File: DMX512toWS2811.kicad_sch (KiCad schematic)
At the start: 74 parts, among them IC1 MAX485ESA+, IC2 MAX485ESA+, IC3 YDS-205, IC4 TLP2361_TPL,E, IC5 MAX485ESA+, IC6 PIC18F27Q43-I_SO, IC7 HD74LV541AT-E, J1 7810-8P8C, J2 7810-8P8C, J3 7810-8P8C, J4 18742, J5 TB112-2-2-E-1, J6 TB112-2-2-E-1, J7 TB111-2-3-U-1-1, U1 FUC-03A, U2 FUC-03A, U3 ERZV07D220, X1 CXO_DIP8

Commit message: * バッテリー監視追加
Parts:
- added C19: 100u, symbol Device:C_Polarized
- added J8: B6B-PH-K-S_LF__SN_, SHDR6W50P0X200_1X6_1390X450X600P, symbol SamacSys_Parts:B6B-PH-K-S_LF__SN_
- added J9: TB112-2-2-E-1, TB11222E1, symbol SamacSys_Parts:TB112-2-2-E-1
- added PS2: BP5293-50, TO254P570X1700X1780-3P, symbol SamacSys_Parts:BP5293-50
- added R22, R23: 1k, symbol Device:R
- added TP1, TP12, TP13, TP14, TP15, TP16, TP17, TP2, TP3, TP4, TP5, TP6, TP7, TP9: TestPoint, symbol Connector:TestPoint
- R1, R16, R2, R20, R5, R6, R7: value R -> 100
- R10, R12, R14, R18: value R -> 1k
- R15, R17, R19, R21, R3, R4, R9: value R -> 10k
- R8: value R -> 300
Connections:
- net +5V: now also J8.2, PS2.3 (VOUT)
- net +BATT: now also J9.1
- net GND: now also C18.1, C2.1, C3.1, IC3.1 (VIN), J5.1, L3.2, LED2.1, C19.2, J8.3, J9.2, PS2.1 (VIN), PS2.2 (GND), R22.1, R23.2
- net ICSPCLK: now also J8.5
- net ICSPDAT: now also J8.4
- net RESET: now also J8.1
- net at IC7.1 (~{OE1}), R19.2: now also IC6.15 (RC4)
- net at C6.1, C7.1, L1.1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: now also C19.1
- net at IC6.10 (RA6): now also TP7.1
- net at IC6.11 (RC0): now also R22.2, R23.1
- net at IC6.12 (RC1): now also TP9.1
- net at IC6.13 (RC2): now also R12.1
- net at IC6.14 (RC3): now also R14.2
- net at IC6.2 (RA0): now also TP1.1
- net at IC6.21 (RB0): now also TP12.1
- net at IC6.22 (RB1): now also TP13.1
- net at IC6.23 (RB2): now also TP14.1
- net at IC6.24 (RB3): now also TP15.1
- net at IC6.25 (RB4): now also TP16.1
- net at IC6.26 (RB5): now also TP17.1
- net at IC6.3 (RA1): now also TP2.1
- net at IC6.4 (RA2): now also TP3.1
- net at IC6.5 (RA3): now also TP4.1
- net at IC6.6 (RA4): now also TP5.1
- net at IC6.7 (RA5): now also TP6.1
- net VDC: no longer names the net of L3.1, U2.1, U2.2, U3.1
- net VDC: no longer C18.1, J5.1
- no-connect marks 25 -> 26
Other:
- moved on the sheet: L1, LED2, LED4, R12, R14, R19, S1, S2

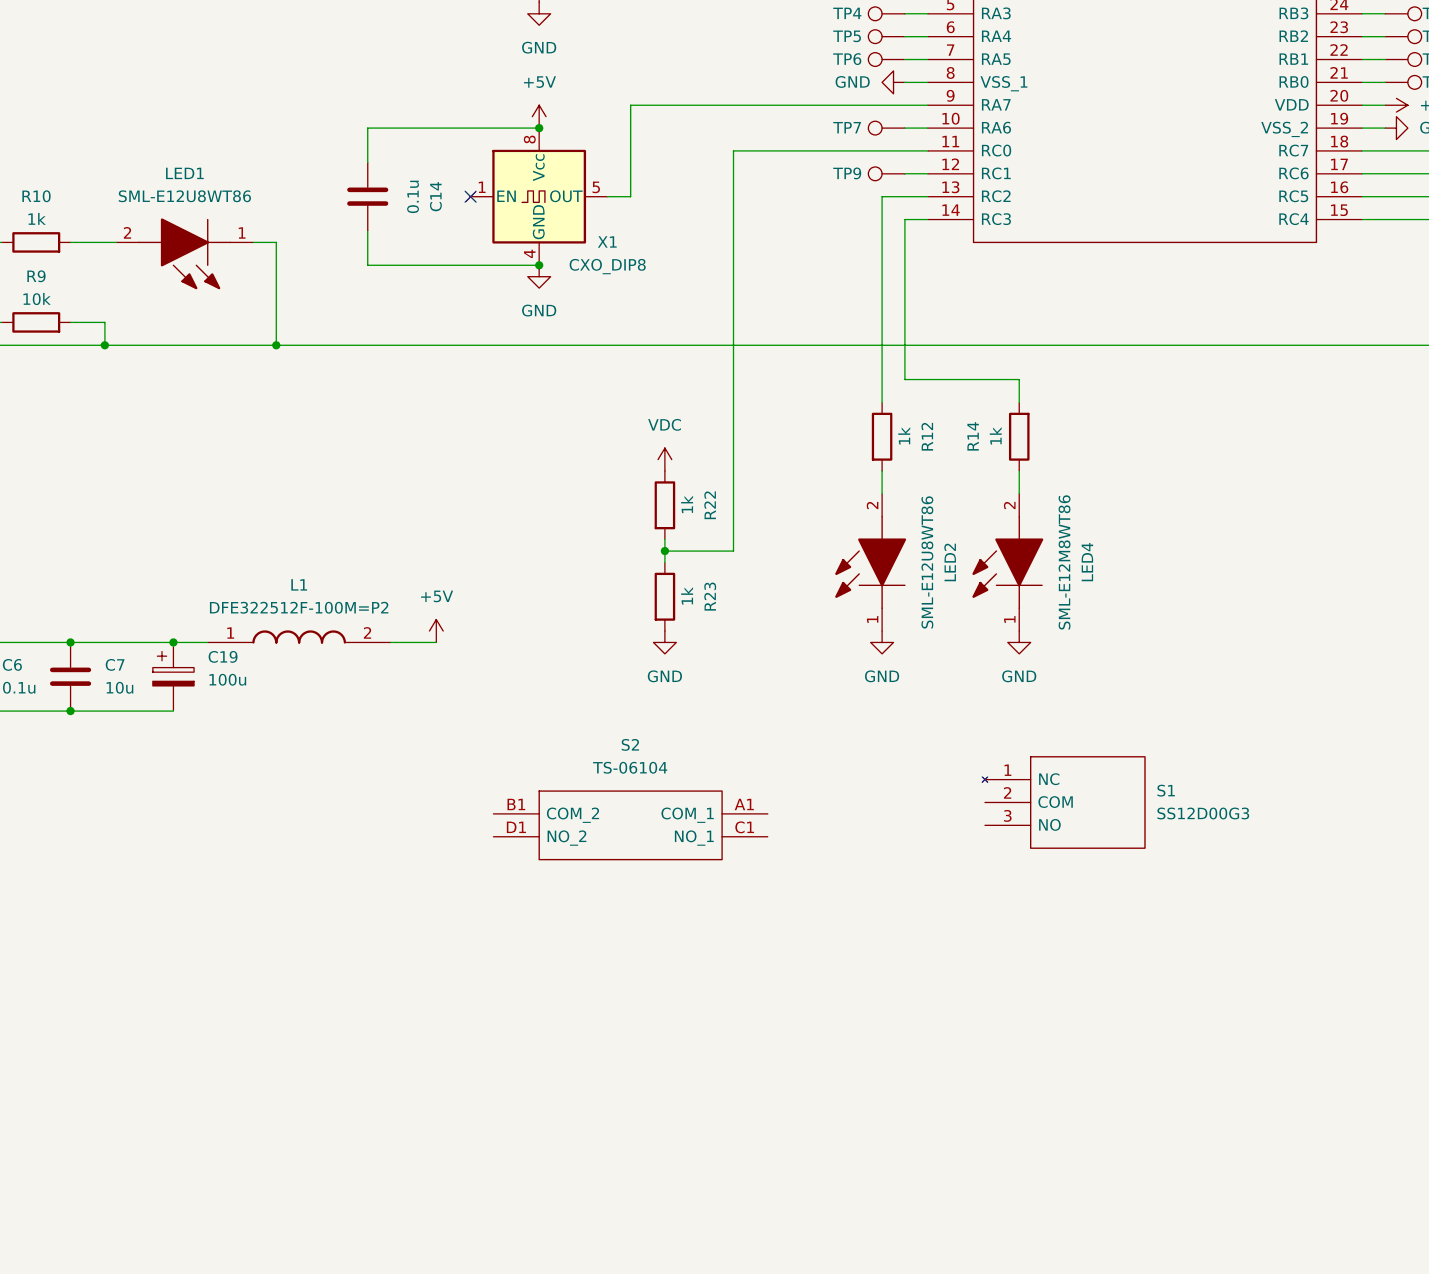
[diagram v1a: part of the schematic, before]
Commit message: * 動作モード切り替えスイッチの追加
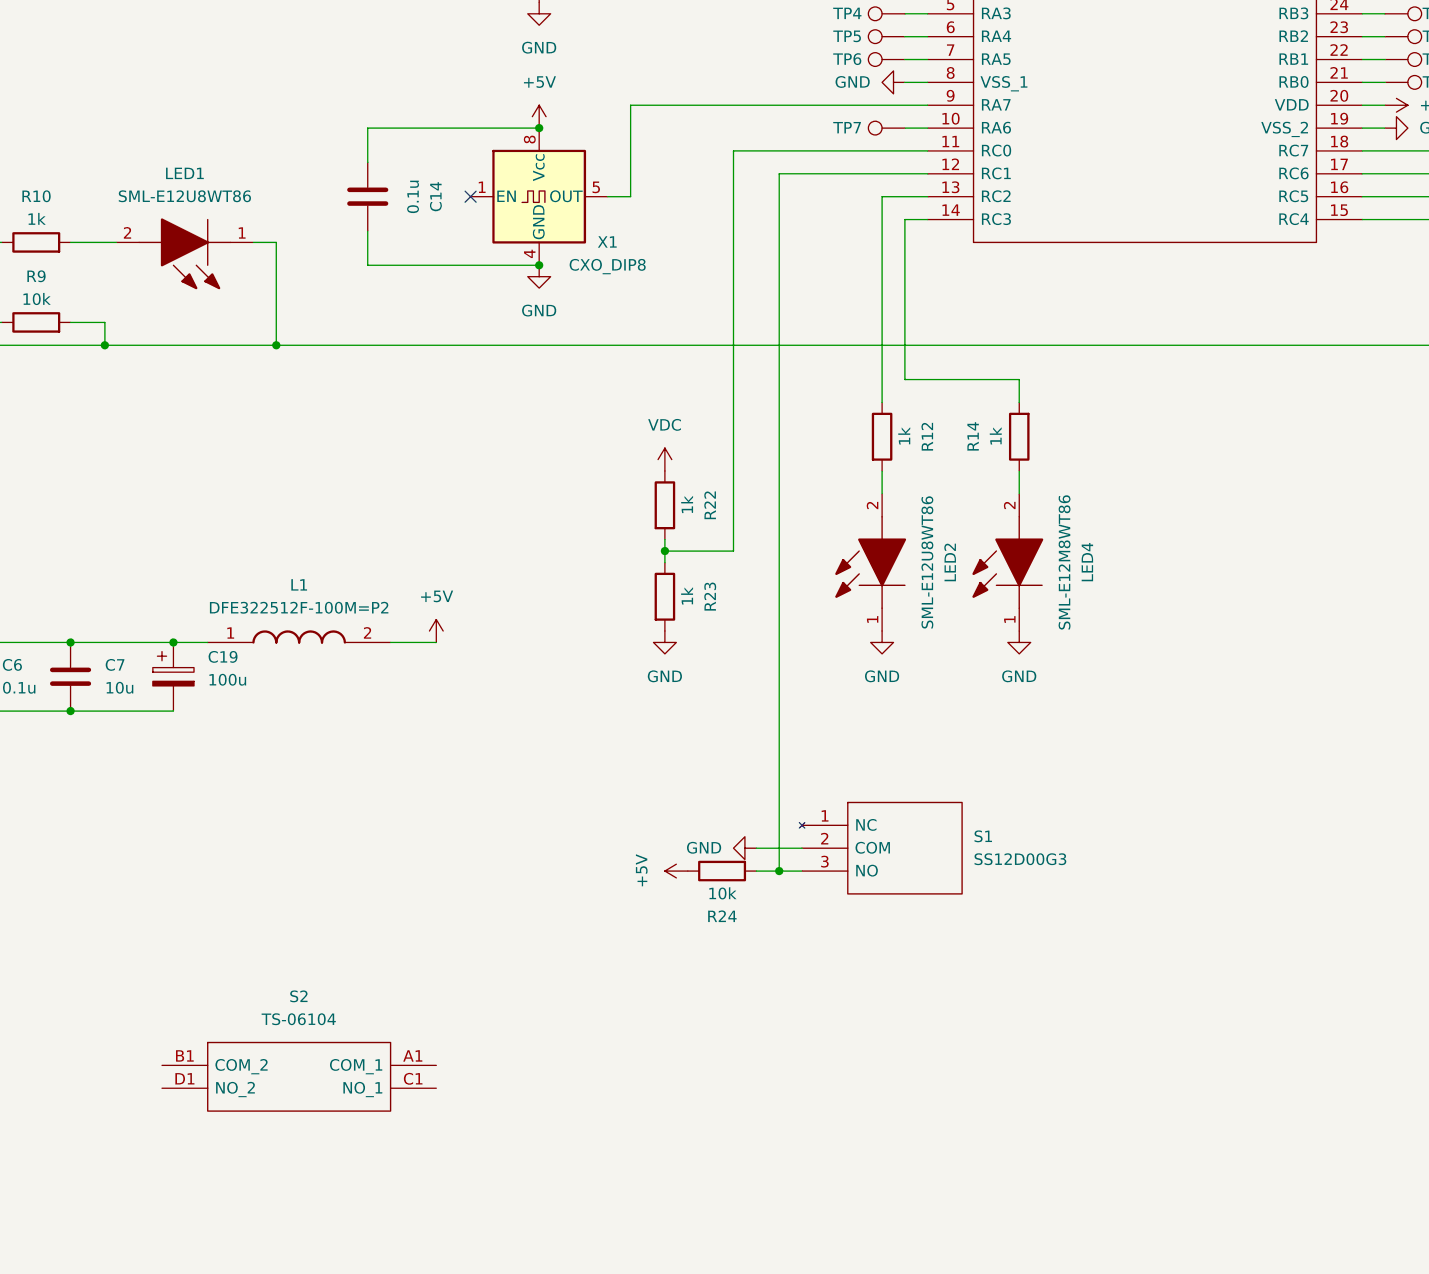
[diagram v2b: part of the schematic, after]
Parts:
- removed TP9: TestPoint, symbol Connector:TestPoint
- added R24: 10k, symbol Device:R
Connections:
- net +5V: now also R24.1
- net GND: now also S1.2 (COM)
- net at IC6.12 (RC1): now also S1.3 (NO), R24.2
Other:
- moved on the sheet: S1, S2

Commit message: * 外部電源供給回路にSWを追加     * MOSFETに逆流時の寄生ダイオード保護のためのダイオードを追加したほうがいいかも * リセットSW､モード切り替えSWを修正
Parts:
- removed C17: 1000u, symbol Device:C_Polarized
- removed TP1, TP12, TP13: TestPoint, symbol Connector:TestPoint
- added C20: 1000u, symbol Device:C_Polarized
- added Q1, Q2: TJ60S04M3L, TJ60S04M3L, symbol SamacSys_Parts:TJ60S04M3L
- added R25: 10k, symbol Device:R
- added R26, R29: 100, symbol Device:R
- added R27, R28, R30: 100k, symbol Device:R
- R13: value R -> 1k
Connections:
- net +5V: now also R25.1; no longer J7.1
- net GND: now also S2.C1 (NO_1), S2.D1 (NO_2), C20.1, C20.2, Q1.3 (S), Q2.3 (S), R27.1, R28.1, R30.2; no longer J5.1
- net at R22.2, R23.1: now also IC6.2 (RA0); no longer IC6.11 (RC0)
- net at IC6.21 (RB0): now also R26.1
- net at IC6.22 (RB1): now also R29.1
- net at S2.A1 (COM_1): now also IC6.11 (RC0), S2.B1 (COM_2), R25.2
- new net: Q2.1 (G), R28.2, R29.2, R30.1
- new net: J5.1, Q2.2 (D)
- new net: Q1.1 (G), R26.2, R27.2
- new net: J7.1, Q1.2 (D)
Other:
- moved on the sheet: C1, C10, C11, C12, C13, C14, C15, C16, C18, C19, C2, C3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

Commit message: * 大まかに配線完了
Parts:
- removed C2, C20: 1000u, symbol Device:C_Polarized
- removed IC3: YDS-205, YDS205, symbol SamacSys_Parts:YDS-205
- removed L3: DFE322512F-100M=P2, 1277ASH100MP2, symbol SamacSys_Parts:DFE322512F-100M=P2
- removed PS2: BP5293-50, TO254P570X1700X1780-3P, symbol SamacSys_Parts:BP5293-50
- removed R20: 100, symbol Device:R
- removed TP15, TP16, TP17, TP3, TP7: TestPoint, symbol Connector:TestPoint
- added C13, C14, C15, C16: 0.1u, Capacitor_SMD:C_0603_1608Metric_Pad1.08x0.95mm_HandSolder, symbol Device:C
- added C6: 4700p, Capacitor_THT:C_Disc_D12.5mm_W5.0mm_P10.00mm, symbol Device:C
- added CA1: 330u, Capacitor_THT:CP_Radial_D10.0mm_P5.00mm, symbol Device:C_Polarized
- added CA4: 1000u, Capacitor_THT:CP_Radial_D10.0mm_P5.00mm, symbol Device:C_Polarized
- added D4: SMBJ5.0CA, DIONM5436X261N, symbol SamacSys_Parts:SMBJ5.0CA
- added D6, D8: SBR2U30P1-7, SODFL3718X100N, symbol SamacSys_Parts:SBR2U30P1-7
- added F3: NANOSMDC010F-2, FUSC3216X100N, symbol SamacSys_Parts:NANOSMDC010F-2
- added F4, F7: FUC-03A, FUC03A, symbol SamacSys_Parts:FUC-03A
- added FL1, FL2: DLW21SN261SQ2L, DLW21SN121HQ2L, symbol SamacSys_Parts:DLW21SN261SQ2L
- added FL3: BNX022-01B, BNX02201K, symbol SamacSys_Parts:BNX022-01B
- added IC4: TCK106AF,LF, SMV_1, symbol SamacSys_Parts:TCK106AF,LF
- added LED1: SML-E12M8WT86, LEDC1608X46N, symbol SamacSys_Parts:SML-E12M8WT86
- added LED6: OSTBABS4C2B, OSTBABS4C2B, symbol SamacSys_Parts:OSTBABS4C2B
- added NT1, NT2: NetTie_2, NetTie:NetTie-2_SMD_Pad2.0mm, symbol Device:NetTie_2
- added PS2: NID35-5, NID355, symbol SamacSys_Parts:NID35-5
- added Q2: 2SK1062_F_, SSM3K7002CFULF, symbol SamacSys_Parts:2SK1062_F_
- added R11: 150k, Resistor_SMD:R_0603_1608Metric_Pad0.98x0.95mm_HandSolder, symbol Device:R
- added R13, R22, R23, R26, R27, R28: 1k, Resistor_SMD:R_0603_1608Metric_Pad0.98x0.95mm_HandSolder, symbol Device:R
- added R17, R33: 10k, Resistor_SMD:R_0603_1608Metric_Pad0.98x0.95mm_HandSolder, symbol Device:R
- added R34: 100, Resistor_SMD:R_1206_3216Metric_Pad1.30x1.75mm_HandSolder, symbol Device:R
- added R40: 100k, Resistor_SMD:R_0603_1608Metric_Pad0.98x0.95mm_HandSolder, symbol Device:R
- C1: renamed from C12; footprint (none) -> Capacitor_SMD:C_0603_1608Metric_Pad1.08x0.95mm_HandSolder; Manufacturer_Name (none) -> murata; Manufacturer_Part_Number (none) -> GRM188F11H104ZA01
- C10: renamed from C4; footprint (none) -> Capacitor_SMD:C_0603_1608Metric_Pad1.08x0.95mm_HandSolder; Manufacturer_Name (none) -> murata; Manufacturer_Part_Number (none) -> GRM188F11H104ZA01
- C11: renamed from C14; footprint (none) -> Capacitor_SMD:C_0603_1608Metric_Pad1.08x0.95mm_HandSolder; Manufacturer_Name (none) -> murata; Manufacturer_Part_Number (none) -> GRM188F11H104ZA01
- C12: renamed from C13; footprint (none) -> Capacitor_SMD:C_0603_1608Metric_Pad1.08x0.95mm_HandSolder; Manufacturer_Name (none) -> murata; Manufacturer_Part_Number (none) -> GRM188F11H104ZA01
- C17: renamed from C5; footprint (none) -> Capacitor_SMD:C_0603_1608Metric_Pad1.08x0.95mm_HandSolder; Manufacturer_Name (none) -> murata; Manufacturer_Part_Number (none) -> GRM188F11H104ZA01
- C18: renamed from C16; footprint (none) -> Capacitor_SMD:C_0603_1608Metric_Pad1.08x0.95mm_HandSolder; Manufacturer_Name (none) -> murata; Manufacturer_Part_Number (none) -> GRM188F11H104ZA01
- C19: renamed from C15; footprint (none) -> Capacitor_SMD:C_0603_1608Metric_Pad1.08x0.95mm_HandSolder; Manufacturer_Name (none) -> murata; Manufacturer_Part_Number (none) -> GRM188F11H104ZA01
- C2: renamed from C11; footprint (none) -> Capacitor_SMD:C_0603_1608Metric_Pad1.08x0.95mm_HandSolder; Manufacturer_Name (none) -> murata; Manufacturer_Part_Number (none) -> GRM188F11H104ZA01
- C3: renamed from C8; footprint (none) -> Capacitor_SMD:C_0603_1608Metric_Pad1.08x0.95mm_HandSolder; Manufacturer_Name (none) -> murata; Manufacturer_Part_Number (none) -> GRM188F11H104ZA01
- C4: renamed from C9; footprint (none) -> Capacitor_SMD:C_1206_3216Metric_Pad1.33x1.80mm_HandSolder; Manufacturer_Name (none) -> murata; Manufacturer_Part_Number (none) -> GRM31CB31H106KA12
- C5: renamed from C10; footprint (none) -> Capacitor_SMD:C_0603_1608Metric_Pad1.08x0.95mm_HandSolder; Manufacturer_Name (none) -> murata; Manufacturer_Part_Number (none) -> GRM188F11H104ZA01
- C7: renamed from C6; footprint (none) -> Capacitor_SMD:C_0603_1608Metric_Pad1.08x0.95mm_HandSolder; Manufacturer_Name (none) -> murata; Manufacturer_Part_Number (none) -> GRM188F11H104ZA01
- C8: renamed from C3; footprint (none) -> Capacitor_SMD:C_0603_1608Metric_Pad1.08x0.95mm_HandSolder; Manufacturer_Name (none) -> murata; Manufacturer_Part_Number (none) -> GRM188F11H104ZA01
- C9: renamed from C7; footprint (none) -> Capacitor_SMD:C_1206_3216Metric_Pad1.33x1.80mm_HandSolder; Manufacturer_Name (none) -> murata; Manufacturer_Part_Number (none) -> GRM31CB31H106KA12
- CA2: renamed from C19; footprint (none) -> Capacitor_THT:CP_Radial_D6.3mm_P2.50mm; Manufacturer_Name (none) -> Panasonic; Manufacturer_Part_Number (none) -> 16SEPC100M
- CA3: renamed from C1; value 1000u -> 22u; footprint (none) -> Capacitor_THT:CP_Radial_D6.3mm_P2.50mm; Manufacturer_Name (none) -> Panasonic; Manufacturer_Part_Number (none) -> 35SEPF22M
- CA5: renamed from C18; value 1000u -> 330u; footprint (none) -> Capacitor_THT:CP_Radial_D10.0mm_P5.00mm; Manufacturer_Name (none) -> Rubycon; Manufacturer_Part_Number (none) -> 35PZJ330M10X9
- D3: Manufacturer_Name (none) -> ROHM; Manufacturer_Part_Number (none) -> 1SS355VM
- IC3: renamed from IC4; footprint 11-4L1S(5-PIN-SOIC) -> SamacSys_Parts:11-4L1S_5-PIN-SOIC_
- LED2: renamed from LED1; footprint LEDM168X46N -> LEDC1608X46N
- LED4: renamed from LED2; footprint LEDM168X46N -> LEDC1608X46N
- R1, R2: footprint (none) -> Resistor_SMD:R_1206_3216Metric_Pad1.30x1.75mm_HandSolder; Manufacturer_Name (none) -> susumu; Manufacturer_Part_Number (none) -> RG3216P-1000-B-T5
- R10: renamed from R11; footprint (none) -> Resistor_SMD:R_0805_2012Metric_Pad1.20x1.40mm_HandSolder; Manufacturer_Name (none) -> FAITHFUL LINK INDUSTRIAL CORP.; Manufacturer_Part_Number (none) -> RC0603J240R
- R12: renamed from R8; footprint (none) -> Resistor_SMD:R_0603_1608Metric_Pad0.98x0.95mm_HandSolder; Manufacturer_Name (none) -> FAITHFUL LINK INDUSTRIAL CORP.; Manufacturer_Part_Number (none) -> RC0603J300R
- R14: renamed from R10; footprint (none) -> Resistor_SMD:R_0603_1608Metric_Pad0.98x0.95mm_HandSolder; Manufacturer_Name (none) -> FAITHFUL LINK INDUSTRIAL CORP.; Manufacturer_Part_Number (none) -> RC0603J1K
- R15: renamed from R9; footprint (none) -> Resistor_SMD:R_0603_1608Metric_Pad0.98x0.95mm_HandSolder; Manufacturer_Name (none) -> FAITHFUL LINK INDUSTRIAL CORP.; Manufacturer_Part_Number (none) -> RC0603J10K
- R16: renamed from R25; footprint (none) -> Resistor_SMD:R_0603_1608Metric_Pad0.98x0.95mm_HandSolder; Manufacturer_Name (none) -> FAITHFUL LINK INDUSTRIAL CORP.; Manufacturer_Part_Number (none) -> RC0603J10K
- R18: renamed from R15; footprint (none) -> Resistor_SMD:R_0603_1608Metric_Pad0.98x0.95mm_HandSolder; Manufacturer_Name (none) -> FAITHFUL LINK INDUSTRIAL CORP.; Manufacturer_Part_Number (none) -> RC0603J10K
- R19: renamed from R13; footprint (none) -> Resistor_SMD:R_0603_1608Metric_Pad0.98x0.95mm_HandSolder; Manufacturer_Name (none) -> FAITHFUL LINK INDUSTRIAL CORP.; Manufacturer_Part_Number (none) -> RC0603J1K
- R20: renamed from R16; footprint (none) -> Resistor_SMD:R_0603_1608Metric_Pad0.98x0.95mm_HandSolder; Manufacturer_Name (none) -> FAITHFUL LINK INDUSTRIAL CORP.; Manufacturer_Part_Number (none) -> RC0603J100R
- R21: renamed from R24; footprint (none) -> Resistor_SMD:R_0603_1608Metric_Pad0.98x0.95mm_HandSolder; Manufacturer_Name (none) -> FAITHFUL LINK INDUSTRIAL CORP.; Manufacturer_Part_Number (none) -> RC0603J10K
- R24: renamed from R12; footprint (none) -> Resistor_SMD:R_0603_1608Metric_Pad0.98x0.95mm_HandSolder; Manufacturer_Name (none) -> FAITHFUL LINK INDUSTRIAL CORP.; Manufacturer_Part_Number (none) -> RC0603J1K
- R25: renamed from R14; footprint (none) -> Resistor_SMD:R_0603_1608Metric_Pad0.98x0.95mm_HandSolder; Manufacturer_Name (none) -> FAITHFUL LINK INDUSTRIAL CORP.; Manufacturer_Part_Number (none) -> RC0603J1K
- R29: renamed from R21; footprint (none) -> Resistor_SMD:R_0603_1608Metric_Pad0.98x0.95mm_HandSolder; Manufacturer_Name (none) -> FAITHFUL LINK INDUSTRIAL CORP.; Manufacturer_Part_Number (none) -> RC0603J10K
- R3: renamed from R5; footprint (none) -> Resistor_SMD:R_1206_3216Metric_Pad1.30x1.75mm_HandSolder; Manufacturer_Name (none) -> susumu; Manufacturer_Part_Number (none) -> RG3216P-1000-B-T5
- R30: renamed from R19; footprint (none) -> Resistor_SMD:R_0603_1608Metric_Pad0.98x0.95mm_HandSolder; Manufacturer_Name (none) -> FAITHFUL LINK INDUSTRIAL CORP.; Manufacturer_Part_Number (none) -> RC0603J10K
- R31: renamed from R18; footprint (none) -> Resistor_SMD:R_0603_1608Metric_Pad0.98x0.95mm_HandSolder; Manufacturer_Name (none) -> FAITHFUL LINK INDUSTRIAL CORP.; Manufacturer_Part_Number (none) -> RC0603J1K
- R32: renamed from R17; footprint (none) -> Resistor_SMD:R_0603_1608Metric_Pad0.98x0.95mm_HandSolder; Manufacturer_Name (none) -> FAITHFUL LINK INDUSTRIAL CORP.; Manufacturer_Part_Number (none) -> RC0603J10K
- R35: renamed from R26; footprint (none) -> Resistor_SMD:R_0603_1608Metric_Pad0.98x0.95mm_HandSolder; Manufacturer_Name (none) -> FAITHFUL LINK INDUSTRIAL CORP.; Manufacturer_Part_Number (none) -> RC0603J100R
- R36: renamed from R27; footprint (none) -> Resistor_SMD:R_0603_1608Metric_Pad0.98x0.95mm_HandSolder; Manufacturer_Name (none) -> FAITHFUL LINK INDUSTRIAL CORP.; Manufacturer_Part_Number (none) -> RC0603J100K
- R37: renamed from R29; footprint (none) -> Resistor_SMD:R_0603_1608Metric_Pad0.98x0.95mm_HandSolder; Manufacturer_Name (none) -> FAITHFUL LINK INDUSTRIAL CORP.; Manufacturer_Part_Number (none) -> RC0603J100R
- R38: renamed from R30; footprint (none) -> Resistor_SMD:R_0603_1608Metric_Pad0.98x0.95mm_HandSolder; Manufacturer_Name (none) -> FAITHFUL LINK INDUSTRIAL CORP.; Manufacturer_Part_Number (none) -> RC0603J100K
- R39: renamed from R28; footprint (none) -> Resistor_SMD:R_0603_1608Metric_Pad0.98x0.95mm_HandSolder; Manufacturer_Name (none) -> FAITHFUL LINK INDUSTRIAL CORP.; Manufacturer_Part_Number (none) -> RC0603J100K
- R4: renamed from R6; footprint (none) -> Resistor_SMD:R_1206_3216Metric_Pad1.30x1.75mm_HandSolder; Manufacturer_Name (none) -> susumu; Manufacturer_Part_Number (none) -> RG3216P-1000-B-T5
- R5: renamed from R3; footprint (none) -> Resistor_SMD:R_0603_1608Metric_Pad0.98x0.95mm_HandSolder; Manufacturer_Name (none) -> FAITHFUL LINK INDUSTRIAL CORP.; Manufacturer_Part_Number (none) -> RC0603J10K
- R6: renamed from R4; footprint (none) -> Resistor_SMD:R_0603_1608Metric_Pad0.98x0.95mm_HandSolder; Manufacturer_Name (none) -> FAITHFUL LINK INDUSTRIAL CORP.; Manufacturer_Part_Number (none) -> RC0603J10K
- R7: footprint (none) -> Resistor_SMD:R_0603_1608Metric_Pad0.98x0.95mm_HandSolder; Manufacturer_Name (none) -> FAITHFUL LINK INDUSTRIAL CORP.; Manufacturer_Part_Number (none) -> RC0603J100R
- R8: renamed from R22; value 1k -> 470k; footprint (none) -> Resistor_SMD:R_0603_1608Metric_Pad0.98x0.95mm_HandSolder; Manufacturer_Name (none) -> FAITHFUL LINK INDUSTRIAL CORP.; Manufacturer_Part_Number (none) -> RC0603J470K
- R9: renamed from R23; value 1k -> 150k; footprint (none) -> Resistor_SMD:R_0603_1608Metric_Pad0.98x0.95mm_HandSolder; Manufacturer_Name (none) -> FAITHFUL LINK INDUSTRIAL CORP.; Manufacturer_Part_Number (none) -> RC0603J150K
- TP1: renamed from TP4; footprint (none) -> TestPoint:TestPoint_THTPad_D1.5mm_Drill0.7mm
- TP2: renamed from TP14; footprint (none) -> TestPoint:TestPoint_THTPad_D1.5mm_Drill0.7mm
- TP3: renamed from TP6; footprint (none) -> TestPoint:TestPoint_THTPad_D1.5mm_Drill0.7mm
- TP4: renamed from TP2; footprint (none) -> TestPoint:TestPoint_THTPad_D1.5mm_Drill0.7mm
- TP5: footprint (none) -> TestPoint:TestPoint_THTPad_D1.5mm_Drill0.7mm
- X1: Manufacturer_Name (none) -> kyocera; Manufacturer_Part_Number (none) -> KHO-HC1-TS-16.0000M
- renumbered J9 to CN1, J4 to CN2, J8 to CN3, J7 to CN4, J5 to CN5, J6 to CN6, D4 to D5, D5 to D7, U1 to F1, U2 to F2, F1 to F5, F2 to F6, IC2 to IC1, IC5 to IC2, IC6 to IC5, IC7 to IC6, IC1 to IC7, LED4 to LED5, LED5 to LED7, Q2 to Q3, S2 to S1, S1 to S2, U3 to VA1
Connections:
- net +5V: now also Q1.3 (S), R36.1, C13.2, CA4.1, D6.1 (K), IC4.5 (VIN), PS2.1 (+VOUT_1), PS2.2 (+VOUT_2), PS2.3 (+VOUT_3), PS2.4 (+VOUT_4); no longer C1.2, C2.2, C3.1, C4.1, IC1.8 (VCC), IC2.8 (VCC), L1.2, PS1.6 (+VOUT), R10.2, R12.1, R6.1
- net GND: now also C5.1, C13.1, C14.2, C15.2, C16.2, C6.2, CA1.2, CA4.2, D4.1, FL3.4 (CG_1), FL3.5 (CG_2), FL3.6 (CG_3), IC4.2 (GND), LED6.4 (K_BL), LED6.5 (K_GL), LED6.6 (K_RL), NT1.1, NT2.1, PS2.5 (COM_1), PS2.6 (COM_2), Q2.2 (S), R11.2, R17.1, R33.2; no longer C8.1, CA5.1, CN1.2, CN2.2, CN4.3, CN6.2, Q1.3 (S), Q3.3 (S), R36.1, R39.1, R8.1, VA1.2
- net GND_ISO: now also J1.10, J1.9, J2.10, J2.9, J3.10, J3.9, C6.1, LED1.1; no longer C5.1
- net RESET: now also IC5.1 (~{MCLR}/VPP/RE3), R20.2; no longer C12.1, D3.2 (A), R18.2, R20.1
- net at IC5.25 (RB4): now also TP4.1
- net at D1.1, R2.1: now also FL1.1; no longer IC1.6 (A)
- net at D1.2, R1.2: now also FL1.4; no longer IC1.7 (B)
- net PWR_LED: now reaches IC5.3 (RA1)
- net PWR_LED: now also R24.1; no longer TP4.1
- net at R37.2, R38.1: now also Q2.1 (G); no longer Q3.1 (G), R39.2
- net at R16.2, S1.A1 (COM_1), S1.B1 (COM_2): now also R22.1; no longer IC5.11 (RC0)
- net UART_RX: now reaches IC7.4 (DI), R31.1
- net UART_RX: now also IC3.5 (VO_(OUTPUT)), IC5.14 (RC3), LED2.1, R15.2; no longer IC5.17 (RC6)
- net at TP3.1: now also IC5.24 (RB3); no longer IC5.7 (RA5)
- net SIGOUT: now reaches IC6.2 (A1), IC6.3 (A2), IC6.4 (A3), IC6.5 (A4), IC6.6 (A5), IC6.7 (A6), IC6.8 (A7), IC6.9 (A8), R29.1
- net SIGOUT: now also IC5.17 (RC6); no longer IC5.16 (RC5)
- net at F2.1, F2.2, VA1.1: now also FL3.1 (B)
- net SIGOUT_nEN: now reaches IC6.1 (~{OE1}), R30.2
- net SIGOUT_nEN: now also IC5.18 (RC7); no longer IC5.15 (RC4)
- net at IC6.11 (Y8), IC6.12 (Y7), IC6.13 (Y6)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: now also R34.1
- net at Q3.2 (D): now also D8.2 (A), F4.1, F4.2; no longer CN5.1
- net D-_OUT: now reaches F5.2
- net D-_OUT: now also CN5.1; no longer CN5.2
- net 485_nRE: now reaches IC7.2 (~{RE}), R32.2
- net 485_nRE: now also IC5.16 (RC5); no longer IC7.3 (DE)
- net D+_OUT: now reaches F6.2
- net D+_OUT: now also CN6.2; no longer CN6.1
- net BAT_VOL: now reaches IC5.2 (RA0), R8.2, R9.1
- net BAT_VOL: now also C14.1, R11.1
- net at IC5.26 (RB5): now also TP5.1
- net SIG_STS: now reaches IC5.4 (RA2)
- net SIG_STS: now also R25.2
- net 5V_OUT: now reaches Q1.2 (D)
- net 5V_OUT: now also CN4.3, D6.2 (A); no longer CN4.1
- net PSMODE_SW: now reaches IC5.10 (RA6)
- net PSMODE_SW: now also C16.1, R23.2
- net at R21.2, S2.3 (NO): now also R23.1; no longer IC5.12 (RC1)
- net PWM_B: now reaches IC5.13 (RC2)
- net PWM_B: now also R26.1; no longer R24.1
- net 5VOUT_EN: now reaches IC5.21 (RB0), R35.1
- net at IC5.22 (RB1): now also TP1.1; no longer R37.1
- net ISOPS_EN: now reaches IC5.5 (RA3)
- net ISOPS_EN: now also IC4.3 (CONTROL), R17.2; no longer TP1.1
- net RST_SW: now reaches IC5.6 (RA4)
- net RST_SW: now also C15.1, R22.2; no longer TP5.1
- net SIG_OUT: now reaches CN4.2
- net SIG_OUT: now also F3.2
- net at D2.1, R4.1: now also FL2.1; no longer IC2.6 (A)
- net at D2.2, R3.2: now also FL2.4; no longer IC2.7 (B)
- new net: IC4.1 (VOUT), L1.2
- new net: Q3.1 (G), R39.1, R40.1
- new net: Q2.3 (D), R39.2
- new net: D4.2, F3.1, R34.2
- new net: C12.1, D3.2 (A), R18.2, R20.1
- new net: FL1.2, IC1.6 (A)
- new net: FL1.3, IC1.7 (B)
- new net: LED6.2 (A_GL), R27.2
- new net: LED6.3 (A_RL), R28.2
- new net: LED6.1 (A_BL), R26.2
- new net: FL2.2, IC2.6 (A)
- new net: FL2.3, IC2.7 (B)
- new net: LED1.2, R13.1
- new net +5V_ISO: C1.2, C2.2, C3.1, C4.1, IC1.8 (VCC), IC2.8 (VCC), PS1.6 (+VOUT), R10.2, R12.1, R13.2, R6.1
- new net -BATT: CN1.2, CN2.2, FL3.3 (PSG), VA1.2
- new net 485_DE: IC5.15 (RC4), IC7.3 (DE), R33.1
- new net DMXPORTOUT_EN: IC5.7 (RA5), R37.1
- new net GND1: CN6.1, NT2.2
- new net GND2: CN4.1, NT1.2
- new net PWM_G: IC5.12 (RC1), R27.1
- new net PWM_R: IC5.11 (RC0), R28.1
- new net VDC: C8.1, CA1.1, CA5.1, D8.1 (K), FL3.2 (CB), PS2.7 (+VIN_1), PS2.8 (+VIN_2), Q3.3 (S), R40.2, R8.1
- new net VPP: CN5.2, F7.1, F7.2
- no-connect marks 26 -> 21
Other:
- note added: "24V時: 3.3V"
- moved on the sheet: C1, C10, C11, C12, C17, C18, C19, C2, C3, C4, C5, C7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

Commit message: * アートワーク作業中
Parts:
- removed NT1, NT2: NetTie_2, NetTie:NetTie-2_SMD_Pad2.0mm, symbol Device:NetTie_2
- removed TP1, TP2: TestPoint, TestPoint:TestPoint_THTPad_D1.5mm_Drill0.7mm, symbol Connector:TestPoint
- added C20: 0.1u, Capacitor_SMD:C_0603_1608Metric_Pad1.08x0.95mm_HandSolder, symbol Device:C
- added C21: 1000p, Capacitor_SMD:C_0603_1608Metric_Pad1.08x0.95mm_HandSolder, symbol Device:C
- added IC8: NJU77551F-TE1, SOT95P280X130-5N, symbol SamacSys_Parts:NJU77551F-TE1
- added R41, R42: 2k, Resistor_SMD:R_0603_1608Metric_Pad0.98x0.95mm_HandSolder, symbol Device:R
- added R43, R44: 0, Resistor_SMD:R_0603_1608Metric_Pad0.98x0.95mm_HandSolder, symbol Device:R
- added R45, R46: 10k, Resistor_SMD:R_0603_1608Metric_Pad0.98x0.95mm_HandSolder, symbol Device:R
- renumbered TP3 to TP1, TP4 to TP2, TP5 to TP3
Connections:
- net GND1 is gone; now on net GND: CN6.1
- net GND2 is gone; now on net GND: CN4.1
- net +5V: now also C20.2, IC8.5 (V+)
- net GND: now also C20.1, IC8.2 (V-), R44.1
- net SIG_OUT: now also R43.2
- net OSIG_P: now reaches IC5.22 (RB1)
- net OSIG_P: now also R46.1
- net OSIG_N: now reaches IC5.23 (RB2)
- net OSIG_N: now also R45.1
- new net: R41.2, R42.2, R43.1
- new net: IC8.1 (+INPUT), R44.2, R45.2, R46.2
- new net: C21.2, IC8.3 (-INPUT), R42.1
- new net: C21.1, IC8.4 (OUTPUT), R41.1
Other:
- moved on the sheet: C10, C18, C8, CA1, CA3, CA4, CN1, CN2, CN3, CN4, D4, D6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
